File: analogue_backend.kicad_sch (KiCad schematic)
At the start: 34 parts, among them M5 RFShield_TwoPieces, U1 TS3021ILT, U2 AD8691, U3 ISL21080CIH341Z-TK, U3 LTC1865-MS, U5 SN74LVC2G74, U6 AD8691

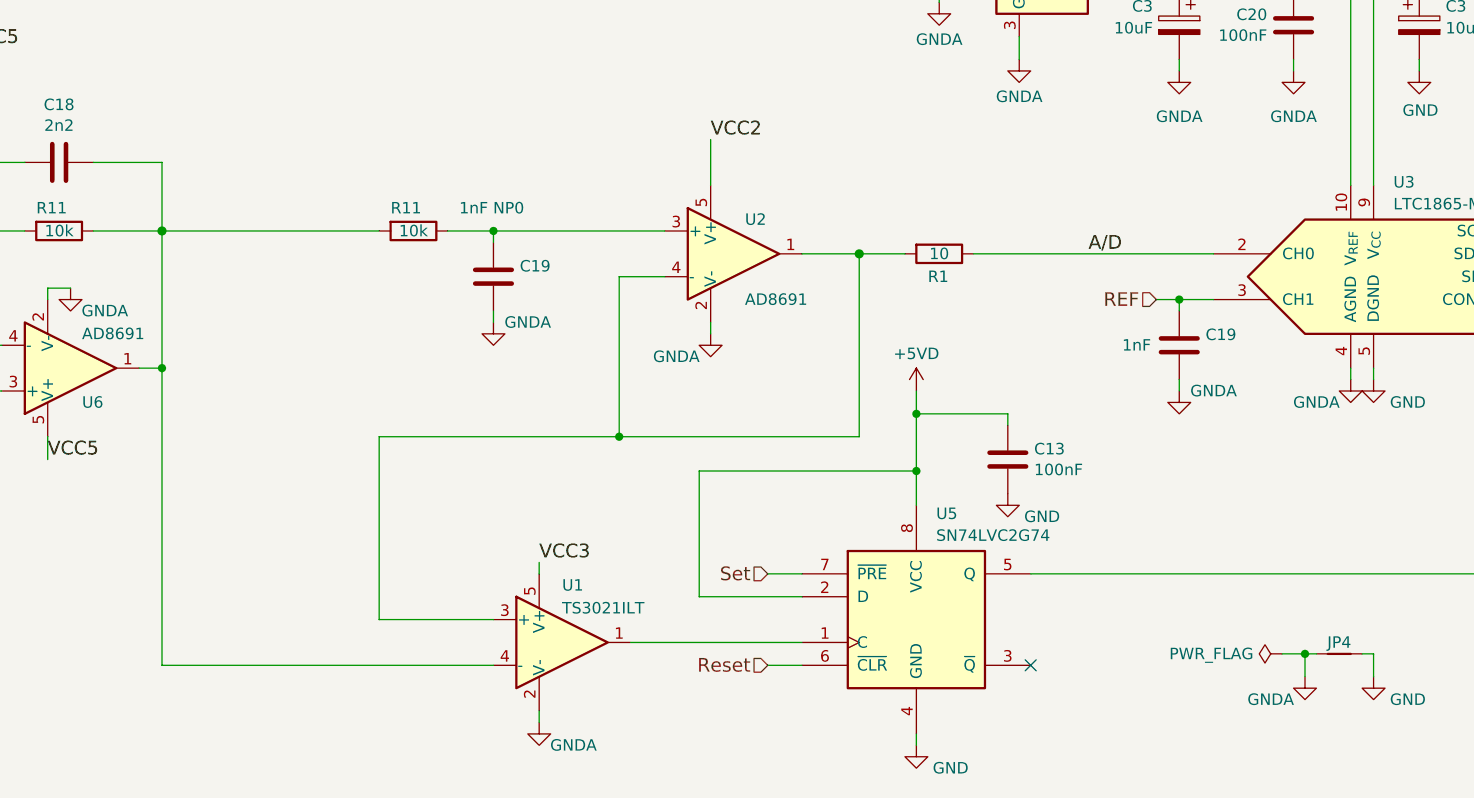
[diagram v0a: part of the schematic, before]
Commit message: Render previews Add testpoints.
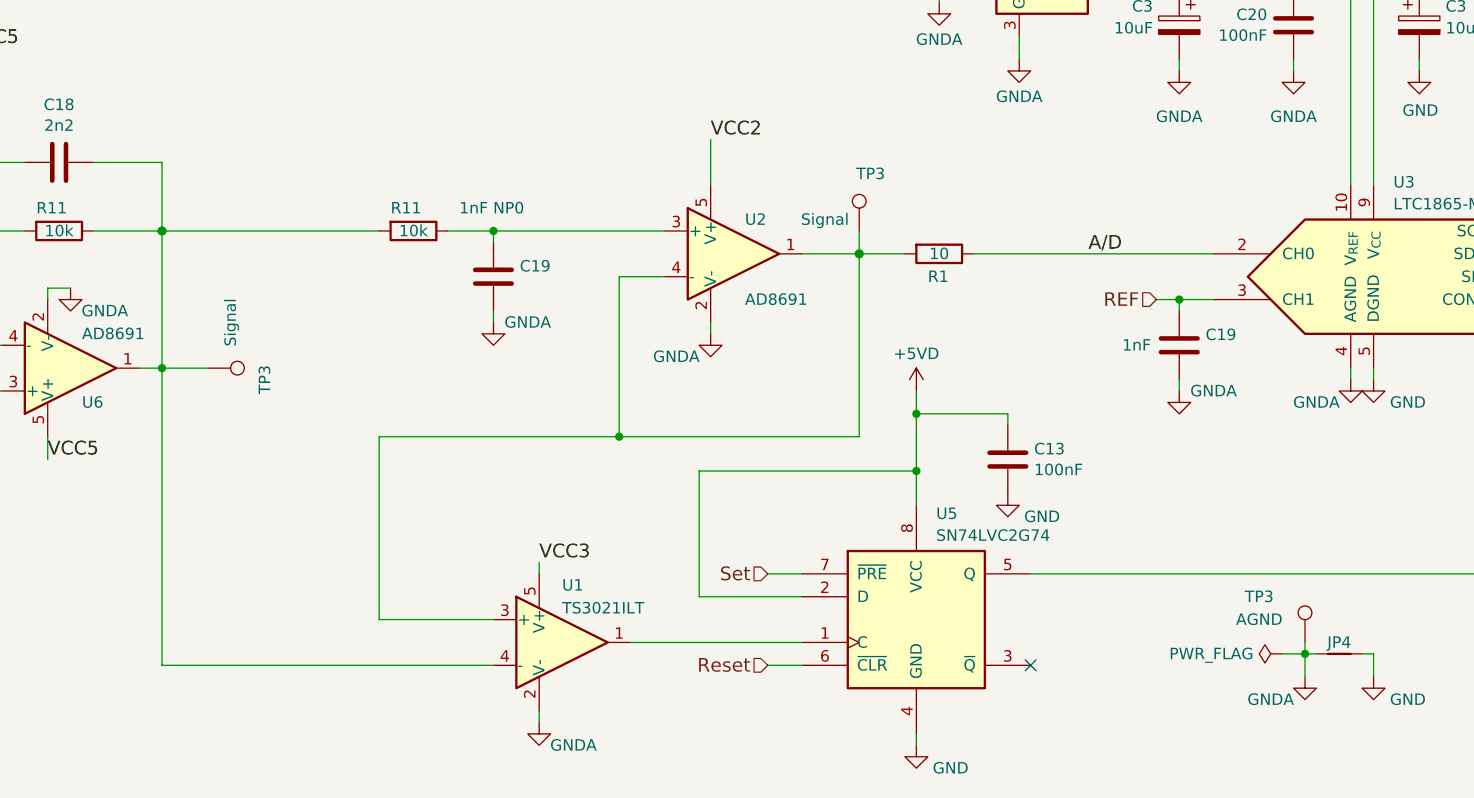
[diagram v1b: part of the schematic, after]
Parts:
- added TP3 (x2): Signal, TestPoint:TestPoint_Pad_D1.0mm, symbol Connector:TestPoint
- added TP3: AGND, TestPoint:TestPoint_Pad_D1.0mm, symbol Connector:TestPoint
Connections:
- net GNDA: now also TP3.1
- net at R1.2, U1.3 (+), U2.1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: now also TP3.1
- net at C18.1, R11.1, R11.2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: now also TP3.1
